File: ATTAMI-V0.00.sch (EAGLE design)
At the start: 23 parts, among them U1 MIC5225, U2 ATTINY85

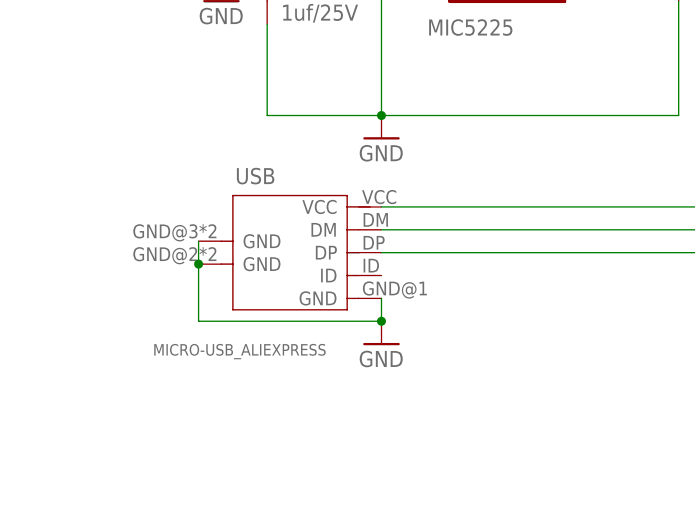
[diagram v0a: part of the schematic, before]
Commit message: ATTami version 0.00
PB5 connected,
Added version # on bnames layer
disconnected usb shield from ground
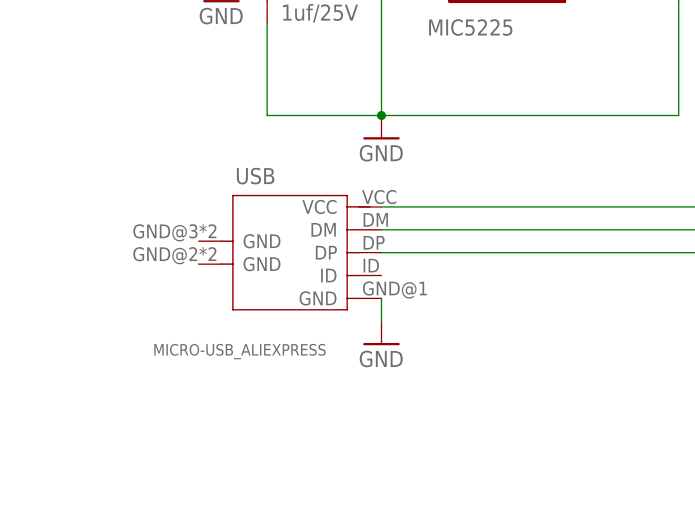
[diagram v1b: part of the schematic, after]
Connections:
- net GND: no longer USB.GND@2, USB.GND@3
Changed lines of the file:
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@@
 </segment>
 <segment>
+<pinref part="GND4" gate="1" pin="GND"/>
 <pinref part="USB" gate="G$1" pin="GND@1"/>
-<pinref part="GND4" gate="1" pin="GND"/>
 <wire x1="63.5" y1="81.28" x2="63.5" y2="78.74" width="0.1524" layer="91"/>
-<pinref part="USB" gate="G$1" pin="GND@2"/>
-<pinref part="USB" gate="G$1" pin="GND@3"/>
-<wire x1="43.18" y1="85.09" x2="43.18" y2="87.63" width="0.1524" layer="91"/>
-<wire x1="43.18" y1="85.09" x2="43.18" y2="78.74" width="0.1524" layer="91"/>
-<wire x1="43.18" y1="78.74" x2="63.5" y2="78.74" width="0.1524" layer="91"/>
-<junction x="43.18" y="85.09"/>
-<junction x="63.5" y="78.74"/>
 </segment>
 <segment>

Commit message: servo shield - new
also added names and labels on wires
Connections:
- net N$1 renamed PB3
- net N$15 renamed PB1
- net N$3 renamed PB0
- net N$5 renamed PB2
- net N$6 renamed PB4
- net N$8 renamed PB5
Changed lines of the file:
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@@
 </segment>
 </net>
-<net name="N$1" class="0">
+<net name="PB3" class="0">
 <segment>
 <wire x1="180.34" y1="88.9" x2="149.86" y2="88.9" width="0.1524" layer="91"/>
@@
 </segment>
 </net>
-<net name="N$3" class="0">
+<net name="PB0" class="0">
 <segment>
 <pinref part="U2" gate="G$1" pin="PB0(MOSI)"/>
@@
 </segment>
 </net>
-<net name="N$5" class="0">
+<net name="PB2" class="0">
 <segment>
 <pinref part="U2" gate="G$1" pin="PB2(SCK/ADC1)"/>
@@
 </segment>
 </net>
-<net name="N$6" class="0">
+<net name="PB4" class="0">
 <segment>
 <pinref part="R4" gate="G$1" pin="2"/>
@@
 </segment>
 </net>
-<net name="N$8" class="0">
+<net name="PB5" class="0">
 <segment>
 <pinref part="U2" gate="G$1" pin="PB5(NRES)"/>
@@
 </segment>
 </net>
-<net name="N$15" class="0">
+<net name="PB1" class="0">
 <segment>
 <pinref part="U2" gate="G$1" pin="PB1(MISO)"/>

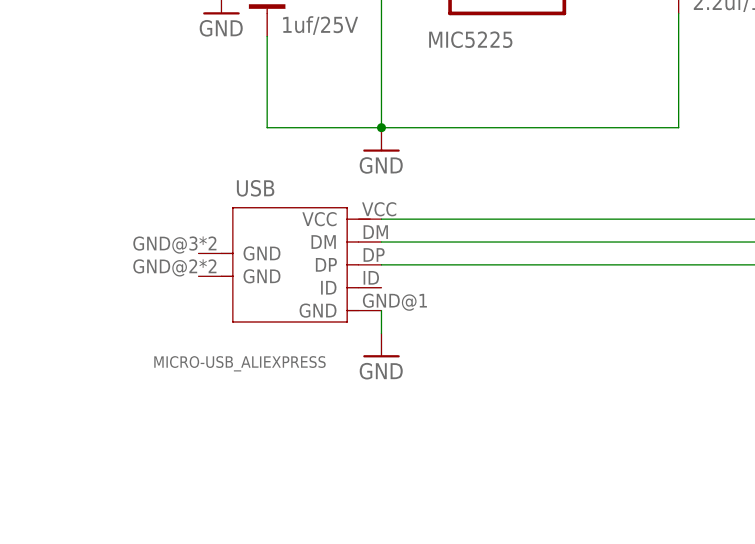
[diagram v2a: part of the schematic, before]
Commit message: removed unuised ID pin from micro usb connector
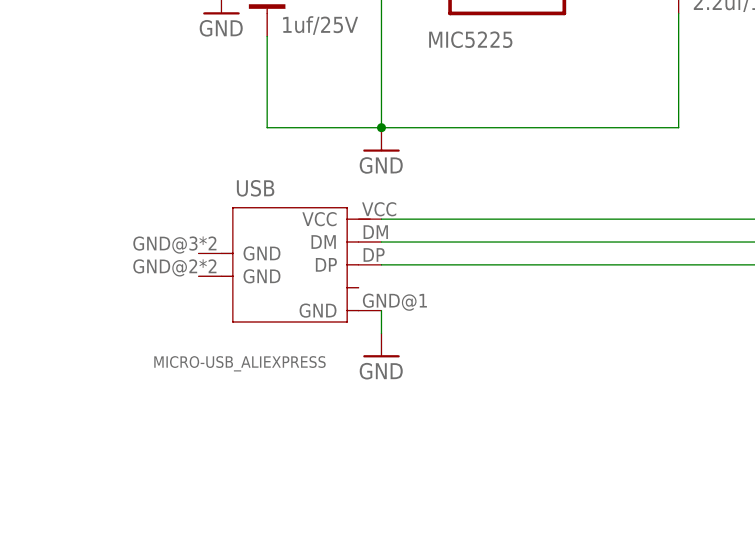
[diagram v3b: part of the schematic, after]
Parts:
- USB: device yair_r:MICRO-USB_ALIEXPRESS -> ATtami:MICRO-USB_ALIEXPRESS
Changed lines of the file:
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@@
 <grid distance="0.1" unitdist="inch" unit="inch" style="lines" multiple="1" display="no" altdistance="0.01" altunitdist="inch" altunit="inch"/>
 <layers>
-<layer number="1" name="Top" color="4" fill="1" visible="no" active="no"/>
-<layer number="2" name="Route2" color="1" fill="3" visible="no" active="no"/>
-<layer number="3" name="Route3" color="4" fill="3" visible="no" active="no"/>
-<layer number="4" name="Route4" color="1" fill="4" visible="no" active="no"/>
-<layer number="5" name="Route5" color="4" fill="4" visible="no" active="no"/>
-<layer number="6" name="Route6" color="1" fill="8" visible="no" active="no"/>
-<layer number="7" name="Route7" color="4" fill="8" visible="no" active="no"/>
-<layer number="8" name="Route8" color="1" fill="2" visible="no" active="no"/>
-<layer number="9" name="Route9" color="4" fill="2" visible="no" active="no"/>
-<layer number="10" name="Route10" color="1" fill="7" visible="no" active="no"/>
-<layer number="11" name="Route11" color="4" fill="7" visible="no" active="no"/>
-<layer number="12" name="Route12" color="1" fill="5" visible="no" active="no"/>
-<layer number="13" name="Route13" color="4" fill="5" visible="no" active="no"/>
-<layer number="14" name="Route14" color="1" fill="6" visible="no" active="no"/>
-<layer number="15" name="Route15" color="4" fill="6" visible="no" active="no"/>
-<layer number="16" name="Bottom" color="1" fill="1" visible="no" active="no"/>
-<layer number="17" name="Pads" color="2" fill="1" visible="no" active="no"/>
-<layer number="18" name="Vias" color="2" fill="1" visible="no" active="no"/>
-<layer number="19" name="Unrouted" color="6" fill="1" visible="no" active="no"/>
-<layer number="20" name="Dimension" color="15" fill="1" visible="no" active="no"/>
-<layer number="21" name="tPlace" color="7" fill="1" visible="no" active="no"/>
-<layer number="22" name="bPlace" color="7" fill="1" visible="no" active="no"/>
-<layer number="23" name="tOrigins" color="15" fill="1" visible="no" active="no"/>
-<layer number="24" name="bOrigins" color="15" fill="1" visible="no" active="no"/>
-<layer number="25" name="tNames" color="7" fill="1" visible="no" active="no"/>
-<layer number="26" name="bNames" color="7" fill="1" visible="no" active="no"/>
-<layer number="27" name="tValues" color="7" fill="1" visible="no" active="no"/>
-<layer number="28" name="bValues" color="7" fill="1" visible="no" active="no"/>
+<layer number="1" name="Top" color="4" fill="1" visible="yes" active="no"/>
+<layer number="2" name="Route2" color="1" fill="3" visible="yes" active="no"/>
+<layer number="3" name="Route3" color="4" fill="3" visible="yes" active="no"/>
+<layer number="4" name="Route4" color="1" fill="4" visible="yes" active="no"/>
+<layer number="5" name="Route5" color="4" fill="4" visible="yes" active="no"/>
+<layer number="6" name="Route6" color="1" fill="8" visible="yes" active="no"/>
+<layer number="7" name="Route7" color="4" fill="8" visible="yes" active="no"/>
+<layer number="8" name="Route8" color="1" fill="2" visible="yes" active="no"/>
+<layer number="9" name="Route9" color="4" fill="2" visible="yes" active="no"/>
+<layer number="10" name="Route10" color="1" fill="7" visible="yes" active="no"/>
+<layer number="11" name="Route11" color="4" fill="7" visible="yes" active="no"/>
+<layer number="12" name="Route12" color="1" fill="5" visible="yes" active="no"/>
+<layer number="13" name="Route13" color="4" fill="5" visible="yes" active="no"/>
+<layer number="14" name="Route14" color="1" fill="6" visible="yes" active="no"/>
+<layer number="15" name="Route15" color="4" fill="6" visible="yes" active="no"/>
+<layer number="16" name="Bottom" color="1" fill="1" visible="yes" active="no"/>
+<layer number="17" name="Pads" color="2" fill="1" visible="yes" active="no"/>
+<layer number="18" name="Vias" color="2" fill="1" visible="yes" active="no"/>
+<layer number="19" name="Unrouted" color="6" fill="1" visible="yes" active="no"/>
+<layer number="20" name="Dimension" color="15" fill="1" visible="yes" active="no"/>
+<layer number="21" name="tPlace" color="7" fill="1" visible="yes" active="no"/>
+<layer number="22" name="bPlace" color="7" fill="1" visible="yes" active="no"/>
+<layer number="23" name="tOrigins" color="15" fill="1" visible="yes" active="no"/>
+<layer number="24" name="bOrigins" color="15" fill="1" visible="yes" active="no"/>
+<layer number="25" name="tNames" color="7" fill="1" visible="yes" active="no"/>
+<layer number="26" name="bNames" color="7" fill="1" visible="yes" active="no"/>
+<layer number="27" name="tValues" color="7" fill="1" visible="yes" active="no"/>
+<layer number="28" name="bValues" color="7" fill="1" visible="yes" active="no"/>
 <layer number="29" name="tStop" color="7" fill="3" visible="no" active="no"/>
 <layer number="30" name="bStop" color="7" fill="6" visible="no" active="no"/>
@@
 <layer number="35" name="tGlue" color="7" fill="4" visible="no" active="no"/>
 <layer number="36" name="bGlue" color="7" fill="5" visible="no" active="no"/>
-<layer number="37" name="tTest" color="7" fill="1" visible="no" active="no"/>
-<layer number="38" name="bTest" color="7" fill="1" visible="no" active="no"/>
+<layer number="37" name="tTest" color="7" fill="1" visible="yes" active="no"/>
+<layer number="38" name="bTest" color="7" fill="1" visible="yes" active="no"/>
 <layer number="39" name="tKeepout" color="4" fill="11" visible="no" active="no"/>
 <layer number="40" name="bKeepout" color="1" fill="11" visible="no" active="no"/>
@@
 <layer number="44" name="Drills" color="7" fill="1" visible="no" active="no"/>
 <layer number="45" name="Holes" color="7" fill="1" visible="no" active="no"/>
-<layer number="46" name="Milling" color="3" fill="1" visible="no" active="no"/>
-<layer number="47" name="Measures" color="7" fill="1" visible="no" active="no"/>
-<layer number="48" name="Document" color="7" fill="1" visible="no" active="no"/>
-<layer number="49" name="Reference" color="7" fill="1" visible="no" active="no"/>
-<layer number="50" name="dxf" color="7" fill="1" visible="no" active="no"/>
-<layer number="51" name="tDocu" color="7" fill="1" visible="no" active="no"/>
-<layer number="52" name="bDocu" color="7" fill="1" visible="no" active="no"/>
-<layer number="53" name="tGND_GNDA" color="7" fill="9" visible="no" active="no"/>
-<layer number="54" name="bGND_GNDA" color="1" fill="9" visible="no" active="no"/>
-<layer number="56" name="wert" color="7" fill="1" visible="no" active="no"/>
+<layer number="46" name="Milling" color="3" fill="1" visible="yes" active="no"/>
+<layer number="47" name="Measures" color="7" fill="1" visible="yes" active="no"/>
+<layer number="48" name="Document" color="7" fill="1" visible="yes" active="no"/>
+<layer number="49" name="Reference" color="7" fill="1" visible="yes" active="no"/>
+<layer number="50" name="dxf" color="7" fill="1" visible="yes" active="no"/>
+<layer number="51" name="tDocu" color="7" fill="1" visible="yes" active="no"/>
+<layer number="52" name="bDocu" color="7" fill="1" visible="yes" active="no"/>
+<layer number="53" name="tGND_GNDA" color="7" fill="9" visible="yes" active="no"/>
+<layer number="54" name="bGND_GNDA" color="1" fill="9" visible="yes" active="no"/>
+<layer number="56" name="wert" color="7" fill="1" visible="yes" active="no"/>
+<layer number="90" name="Modules" color="5" fill="1" visible="yes" active="yes"/>
 <layer number="91" name="Nets" color="2" fill="1" visible="yes" active="yes"/>
 <layer number="92" name="Busses" color="1" fill="1" visible="yes" active="yes"/>
@@
 <part name="U$1" library="microbuilder" deviceset="MOUNTINGHOLE" device="2.0" value="MOUNTINGHOLE2.0"/>
 <part name="S1" library="SparkFun-Electromechanical" deviceset="SWITCH-MOMENTARY-2" device="-SMD-1101NE"/>
-<part name="USB" library="yair_r" deviceset="MICRO-USB_ALIEXPRESS" device=""/>
+<part name="USB" library="ATtami" deviceset="MICRO-USB_ALIEXPRESS" device=""/>
 <part name="GND4" library="SparkFun" deviceset="GND" device=""/>
 <part name="U$2" library="microbuilder" deviceset="MOUNTINGHOLE" device="2.0" value="MOUNTINGHOLE2.0"/>

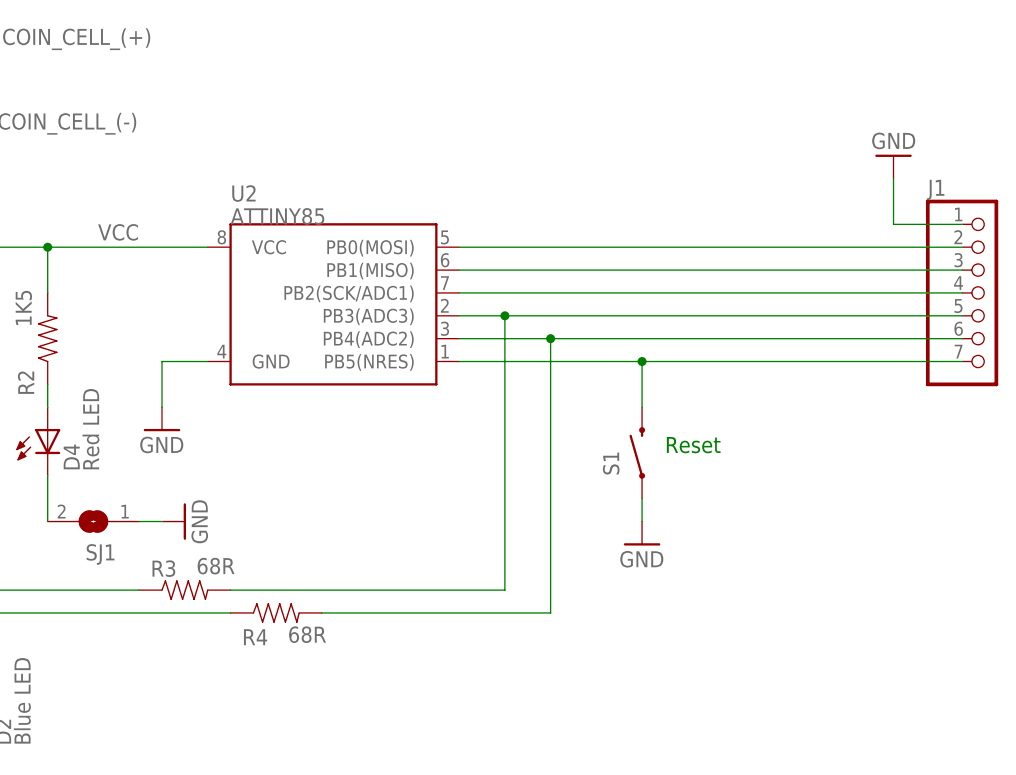
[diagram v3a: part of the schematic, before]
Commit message: moved all parts to ATtami lib, trimmed it
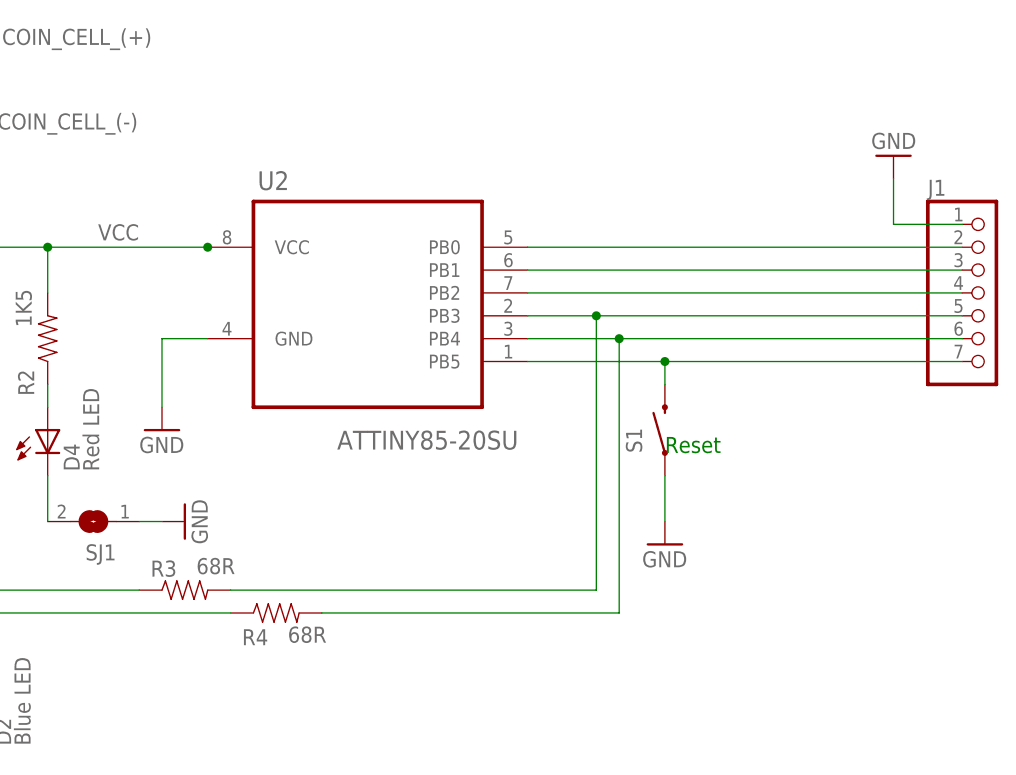
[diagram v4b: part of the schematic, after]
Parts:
- C1, C2: device SparkFun:CAP0805 -> ATtami:CAP0805
- COIN_CELL_(+), COIN_CELL_(-): device adafruit:PINHD-1X1CB -> ATtami:PINHD-1X1
- D1, D2, D4: device dp_devices:LED-0805 -> ATtami:LED-0805
- D3, D5: device microbuilder:DIODESOD-323 -> ATtami:SCHOTTKY-DIODESOD-323
- J1: device microbuilder:HEADER-1X7ROUND -> ATtami:HEADER-1X7ROUND
- J2, J3: device microbuilder:HEADER-1X2ROUND -> ATtami:HEADER-1X2ROUND
- R1, R2, R3, R4: device SparkFun:RESISTOR0805-RES -> ATtami:RESISTOR0805-RES
- S1: device SparkFun-Electromechanical:SWITCH-MOMENTARY-2-SMD-1101NE -> ATtami:SWITCH-MOMENTARY-2-SMD-1101NE
- SJ1: device microbuilder:SOLDERJUMPERCLOSED -> ATtami:SOLDERJUMPERCLOSED
- U$1, U$2: device microbuilder:MOUNTINGHOLE2.0 -> ATtami:MOUNTINGHOLE2.0
- U1: device SparkFun:V_REG_LDOSMD -> ATtami:V_REG_LDOSMD
- U2: value ATTINY85 -> ATTINY85-20SU; device SparkFun:ATTINY45 -> ATtami:ATTINY85-20SU
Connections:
- net PB0: now also U2.PB0; no longer U2.PB0(MOSI)
- net PB1: now also U2.PB1; no longer U2.PB1(MISO)
- net PB2: now also U2.PB2; no longer U2.PB2(SCK/ADC1)
- net PB3: now also U2.PB3; no longer U2.PB3(ADC3)
- net PB4: now also U2.PB4; no longer U2.PB4(ADC2)
- net PB5: now also U2.PB5; no longer U2.PB5(NRES)
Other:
- moved on the sheet: S1
